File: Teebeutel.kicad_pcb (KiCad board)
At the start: 2 copper layers, 40 x 55.7 mm, 66 parts, among them J1 RJ45_Shielded, J2 Conn_01x30_Female, J3 Micro_SD_Card, Q1 S8050, Q2 S8050, SW1 K1-1506SN-01, U1 ESP32-WROOM-32, U2 TLV1117-33, U3 MCP73831-2-OT, U4 SDB628, U5 LIS2DE12, U6 TLV70018_SOT23-5, U7 SGP30, U8 PPSI262, U9 TXB0104RUT

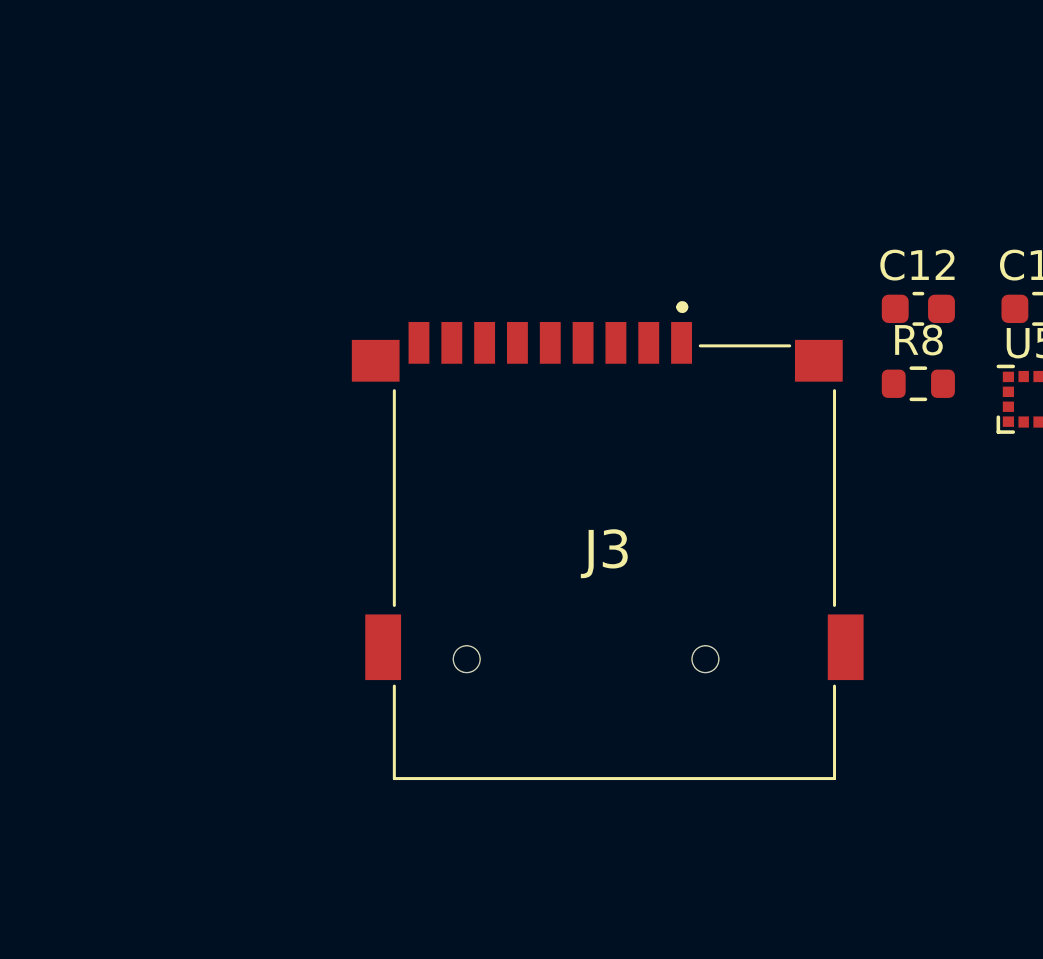
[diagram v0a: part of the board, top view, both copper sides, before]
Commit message: fix: Move pulldown R in the Boot-mode selector
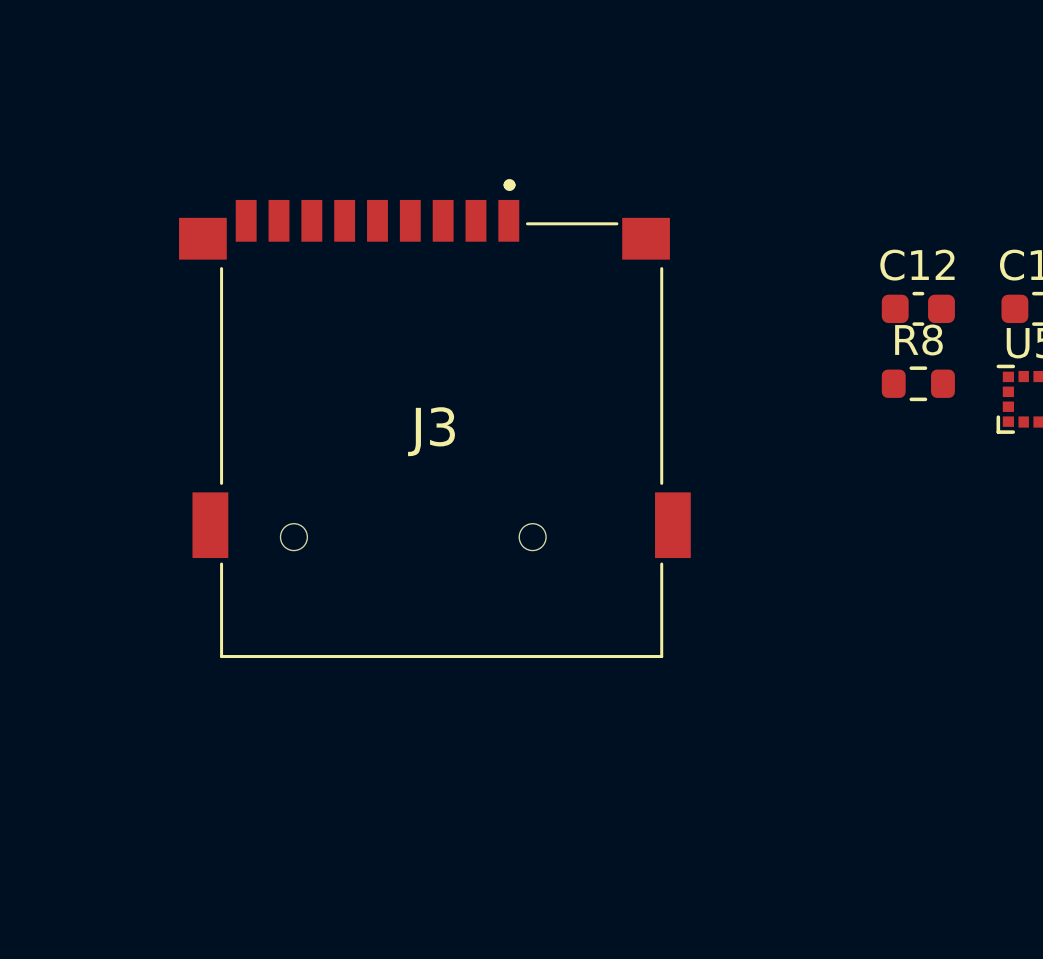
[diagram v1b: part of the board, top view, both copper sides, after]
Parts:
- moved J3 7.09 mm to (109.0, -20.4)
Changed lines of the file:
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@@
     (add_net WS2812)
+  )
+  (module custom_parts:TF15X15 (layer F.Cu)
+    (at 109 -20.4)
+    (descr TF-15X15-4)
+    (tags Connector)
+    (fp_text reference J3 (at 0 0) (layer F.SilkS)
+      (effects (font (size 1.27 1.27) (thickness 0.254)))
+    )
+    (fp_text value Micro_SD_Card (at 0 0) (layer F.SilkS) hide
+      (effects (font (size 1.27 1.27) (thickness 0.254)))
+    )
+    (fp_text user %R (at 0 0) (layer F.Fab)
+      (effects (font (size 1.27 1.27) (thickness 0.254)))
+    )
+    (fp_arc (start 2.5 -8.15) (end 2.4 -8.15) (angle -180) (layer F.SilkS) (width 0.2))
+    (fp_arc (start 2.5 -8.15) (end 2.6 -8.15) (angle -180) (layer F.SilkS) (width 0.2))
+    (fp_line (start 2.6 -8.15) (end 2.6 -8.15) (layer F.SilkS) (width 0.2))
+    (fp_line (start 2.4 -8.15) (end 2.4 -8.15) (layer F.SilkS) (width 0.2))
+    (fp_line (start 6.1 -6.85) (end 3.1 -6.85) (layer F.SilkS) (width 0.1))
+    (fp_line (start 7.6 1.85) (end 7.6 -5.35) (layer F.SilkS) (width 0.1))
+    (fp_line (start 7.6 7.65) (end 7.6 4.55) (layer F.SilkS) (width 0.1))
+    (fp_line (start -7.15 7.65) (end 7.6 7.65) (layer F.SilkS) (width 0.1))
+    (fp_line (start -7.15 4.55) (end -7.15 7.65) (layer F.SilkS) (width 0.1))
+    (fp_line (start -7.15 -5.35) (end -7.15 1.85) (layer F.SilkS) (width 0.1))
+    (fp_line (start -9.575 8.65) (end -9.575 -8.65) (layer F.CrtYd) (width 0.1))
+    (fp_line (start 9.575 8.65) (end -9.575 8.65) (layer F.CrtYd) (width 0.1))
+    (fp_line (start 9.575 -8.65) (end 9.575 8.65) (layer F.CrtYd) (width 0.1))
+    (fp_line (start -9.575 -8.65) (end 9.575 -8.65) (layer F.CrtYd) (width 0.1))
+    (fp_line (start -7.15 7.65) (end -7.15 -6.85) (layer F.Fab) (width 0.2))
+    (fp_line (start 7.6 7.65) (end -7.15 7.65) (layer F.Fab) (width 0.2))
+    (fp_line (start 7.6 -6.85) (end 7.6 7.65) (layer F.Fab) (width 0.2))
+    (fp_line (start -7.15 -6.85) (end 7.6 -6.85) (layer F.Fab) (width 0.2))
+    (pad 1 smd rect (at 2.475 -6.95) (size 0.7 1.4) (layers F.Cu F.Paste F.Mask))
+    (pad 2 smd rect (at 1.375 -6.95) (size 0.7 1.4) (layers F.Cu F.Paste F.Mask)
+      (net 29 SD-CS))
+    (pad 3 smd rect (at 0.275 -6.95) (size 0.7 1.4) (layers F.Cu F.Paste F.Mask)
+      (net 28 SD-MOSI))
+    (pad 4 smd rect (at -0.825 -6.95) (size 0.7 1.4) (layers F.Cu F.Paste F.Mask)
+      (net 9 +3V3))
+    (pad 5 smd rect (at -1.925 -6.95) (size 0.7 1.4) (layers F.Cu F.Paste F.Mask)
+      (net 27 SD-SCK))
+    (pad 6 smd rect (at -3.025 -6.95) (size 0.7 1.4) (layers F.Cu F.Paste F.Mask)
+      (net 2 GND))
+    (pad 7 smd rect (at -4.125 -6.95) (size 0.7 1.4) (layers F.Cu F.Paste F.Mask)
+      (net 26 SD-MISO))
+    (pad 8 smd rect (at -5.225 -6.95) (size 0.7 1.4) (layers F.Cu F.Paste F.Mask))
+    (pad 9 smd rect (at -6.325 -6.95) (size 0.7 1.4) (layers F.Cu F.Paste F.Mask)
+      (net 2 GND))
+    (pad 14 np_thru_hole circle (at -4.725 3.65) (size 0.9 0) (drill 0.9) (layers *.Cu *.Mask))
+    (pad 15 np_thru_hole circle (at 3.275 3.65) (size 0.9 0) (drill 0.9) (layers *.Cu *.Mask))
+    (pad MP1 smd rect (at -7.775 -6.35 90) (size 1.4 1.6) (layers F.Cu F.Paste F.Mask))
+    (pad MP2 smd rect (at 7.075 -6.35 90) (size 1.4 1.6) (layers F.Cu F.Paste F.Mask))
+    (pad MP3 smd rect (at -7.525 3.25) (size 1.2 2.2) (layers F.Cu F.Paste F.Mask))
+    (pad MP4 smd rect (at 7.975 3.25) (size 1.2 2.2) (layers F.Cu F.Paste F.Mask))
+    (model ${KIPRJMOD}/custom_parts.pretty/TF-15X15.stp
+      (offset (xyz 0.22 -0.11 0.97))
+      (scale (xyz 1 1 1))
+      (rotate (xyz -90 0 0))
+    )
   )
   (module custom_parts:K1-1506SN-01 (layer F.Cu)
@@
     )
   )
-  (module custom_parts:TF15X15 (layer F.Cu)
-    (at 114.79 -16.31)
-    (descr TF-15X15-4)
-    (tags Connector)
-    (fp_text reference J3 (at 0 0) (layer F.SilkS)
-      (effects (font (size 1.27 1.27) (thickness 0.254)))
-    )
-    (fp_text value Micro_SD_Card (at 0 0) (layer F.SilkS) hide
-      (effects (font (size 1.27 1.27) (thickness 0.254)))
-    )
-    (fp_text user %R (at 0 0) (layer F.Fab)
-      (effects (font (size 1.27 1.27) (thickness 0.254)))
-    )
-    (fp_arc (start 2.5 -8.15) (end 2.4 -8.15) (angle -180) (layer F.SilkS) (width 0.2))
-    (fp_arc (start 2.5 -8.15) (end 2.6 -8.15) (angle -180) (layer F.SilkS) (width 0.2))
-    (fp_line (start 2.6 -8.15) (end 2.6 -8.15) (layer F.SilkS) (width 0.2))
-    (fp_line (start 2.4 -8.15) (end 2.4 -8.15) (layer F.SilkS) (width 0.2))
-    (fp_line (start 6.1 -6.85) (end 3.1 -6.85) (layer F.SilkS) (width 0.1))
-    (fp_line (start 7.6 1.85) (end 7.6 -5.35) (layer F.SilkS) (width 0.1))
-    (fp_line (start 7.6 7.65) (end 7.6 4.55) (layer F.SilkS) (width 0.1))
-    (fp_line (start -7.15 7.65) (end 7.6 7.65) (layer F.SilkS) (width 0.1))
-    (fp_line (start -7.15 4.55) (end -7.15 7.65) (layer F.SilkS) (width 0.1))
-    (fp_line (start -7.15 -5.35) (end -7.15 1.85) (layer F.SilkS) (width 0.1))
-    (fp_line (start -9.575 8.65) (end -9.575 -8.65) (layer F.CrtYd) (width 0.1))
-    (fp_line (start 9.575 8.65) (end -9.575 8.65) (layer F.CrtYd) (width 0.1))
-    (fp_line (start 9.575 -8.65) (end 9.575 8.65) (layer F.CrtYd) (width 0.1))
-    (fp_line (start -9.575 -8.65) (end 9.575 -8.65) (layer F.CrtYd) (width 0.1))
-    (fp_line (start -7.15 7.65) (end -7.15 -6.85) (layer F.Fab) (width 0.2))
-    (fp_line (start 7.6 7.65) (end -7.15 7.65) (layer F.Fab) (width 0.2))
-    (fp_line (start 7.6 -6.85) (end 7.6 7.65) (layer F.Fab) (width 0.2))
-    (fp_line (start -7.15 -6.85) (end 7.6 -6.85) (layer F.Fab) (width 0.2))
-    (pad 1 smd rect (at 2.475 -6.95) (size 0.7 1.4) (layers F.Cu F.Paste F.Mask))
-    (pad 2 smd rect (at 1.375 -6.95) (size 0.7 1.4) (layers F.Cu F.Paste F.Mask)
-      (net 29 SD-CS))
-    (pad 3 smd rect (at 0.275 -6.95) (size 0.7 1.4) (layers F.Cu F.Paste F.Mask)
-      (net 28 SD-MOSI))
-    (pad 4 smd rect (at -0.825 -6.95) (size 0.7 1.4) (layers F.Cu F.Paste F.Mask)
-      (net 9 +3V3))
-    (pad 5 smd rect (at -1.925 -6.95) (size 0.7 1.4) (layers F.Cu F.Paste F.Mask)
-      (net 27 SD-SCK))
-    (pad 6 smd rect (at -3.025 -6.95) (size 0.7 1.4) (layers F.Cu F.Paste F.Mask)
-      (net 2 GND))
-    (pad 7 smd rect (at -4.125 -6.95) (size 0.7 1.4) (layers F.Cu F.Paste F.Mask)
-      (net 26 SD-MISO))
-    (pad 8 smd rect (at -5.225 -6.95) (size 0.7 1.4) (layers F.Cu F.Paste F.Mask))
-    (pad 9 smd rect (at -6.325 -6.95) (size 0.7 1.4) (layers F.Cu F.Paste F.Mask)
-      (net 2 GND))
-    (pad 14 np_thru_hole circle (at -4.725 3.65) (size 0.9 0) (drill 0.9) (layers *.Cu *.Mask))
-    (pad 15 np_thru_hole circle (at 3.275 3.65) (size 0.9 0) (drill 0.9) (layers *.Cu *.Mask))
-    (pad MP1 smd rect (at -7.775 -6.35 90) (size 1.4 1.6) (layers F.Cu F.Paste F.Mask))
-    (pad MP2 smd rect (at 7.075 -6.35 90) (size 1.4 1.6) (layers F.Cu F.Paste F.Mask))
-    (pad MP3 smd rect (at -7.525 3.25) (size 1.2 2.2) (layers F.Cu F.Paste F.Mask))
-    (pad MP4 smd rect (at 7.975 3.25) (size 1.2 2.2) (layers F.Cu F.Paste F.Mask))
-    (model ${KIPRJMOD}/custom_parts.pretty/TF-15X15.stp
-      (offset (xyz 0.22 -0.11 0.97))
-      (scale (xyz 1 1 1))
-      (rotate (xyz -90 0 0))
-    )
-  )

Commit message: feat: alot of stuff
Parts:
- added C20: 100n, Capacitor_SMD:C_0603_1608Metric, F.Cu at (121.8, 131.0)
- added C21: 10µ, Capacitor_SMD:C_0603_1608Metric, F.Cu at (240.5, 47.5)
- added C22: 1µ, Capacitor_SMD:C_0603_1608Metric, F.Cu at (256.1, 34.1)
- added C23: 10µ, Capacitor_SMD:C_0603_1608Metric, F.Cu at (232.1, 58.2)
- added C24: 100n, Capacitor_SMD:C_0603_1608Metric, F.Cu at (236.1, 53.8)
- added C25: 4,7µ, Capacitor_SMD:C_0603_1608Metric, F.Cu at (240.5, 50.0)
- added C26: 4,7µ, Capacitor_SMD:C_0603_1608Metric, F.Cu at (260.7, 29.7)
- added C27: 100n, Capacitor_SMD:C_0603_1608Metric, F.Cu at (121.5, 136.1)
- added C28: 22µF, Capacitor_SMD:C_0603_1608Metric, F.Cu at (246.7, 45.0)
- added C29: 10µ, Capacitor_SMD:C_0603_1608Metric, F.Cu at (252.5, 49.1)
- added C30: 100n, Capacitor_SMD:C_0603_1608Metric, F.Cu at (242.7, 42.5)
- added C31: 22µF, Capacitor_SMD:C_0603_1608Metric, F.Cu at (255.9, 36.6)
- added C32: 10µ, Capacitor_SMD:C_0603_1608Metric, F.Cu at (236.1, 56.3)
- added D10: WS2812B, Teebeutel_Special_Parts:WS2812B-4020, F.Cu at (111.0, 80.0)
- added D11: WS2812B, Teebeutel_Special_Parts:WS2812B-4020, F.Cu at (172.0, 149.0)
- added D12: WS2812B, Teebeutel_Special_Parts:WS2812B-4020, F.Cu at (120.6, 58.0)
- added D13: LED-RED, LED_SMD:LED_1210_3225Metric, F.Cu at (159.9, 52.5)
- added D14: LED-GREEN, LED_SMD:LED_1210_3225Metric, F.Cu at (132.1, 52.5)
- added D15: 1N4148WT, Diode_SMD:D_SOD-523, F.Cu at (272.5, 30.1)
- added D16: 1N4148WT, Diode_SMD:D_SOD-523, F.Cu at (247.9, 55.0)
- added D17: D, Diode_SMD:D_SMA, F.Cu at (212.4, 56.9)
- added G***: LOGO, Teebeutel_Graphics:rotate-orbit, F.Cu at (142.1, 100.0)
- added G***: LOGO, Teebeutel_Graphics:wind, B.Cu at (126.2, 139.2)
- added G***: LOGO, Teebeutel_Graphics:heartbeat, B.Cu at (165.8, 139.2)
- added J4: Conn_01x30_Female, Connector_FFC-FPC:TE_3-84953-0_1x30-1MP_P1.0mm_Horizontal, F.Cu at (146.0, 87.0)
- added R23: 560k, Resistor_SMD:R_0603_1608Metric, F.Cu at (252.5, 46.6)
- added R24: 620k 1%, Resistor_SMD:R_0603_1608Metric, F.Cu at (248.5, 52.5)
- added R25: 30k 1%, Resistor_SMD:R_0603_1608Metric, F.Cu at (268.2, 32.7)
- added SW2: SW_SPST, Button_Switch_SMD:SW_SPDT_PCM12, F.Cu at (113.0, 130.0)
- added TB1: Touch Button 2, Teebeutel_Graphics:Touch-Button_Python, B.Cu at (120.0, 120.0)
- added TB2: Touch Button 2, Teebeutel_Graphics:Touch-Button_OSHW, B.Cu at (172.0, 120.0)
- added TP1: ESP32 EN, TestPoint:TestPoint_Pad_D1.0mm, F.Cu at (262.2, 42.5)
- added TP10: RxD 3.3V, TestPoint:TestPoint_Pad_D1.0mm, F.Cu at (259.1, 48.1)
- added TP11: RTS 3.3V, TestPoint:TestPoint_Pad_D1.0mm, F.Cu at (256.1, 48.1)
- added TP12: Button Right, TestPoint:TestPoint_Pad_D1.0mm, F.Cu at (266.7, 38.5)
- added TP13: I²C SDA, TestPoint:TestPoint_Pad_D1.0mm, F.Cu at (251.2, 55.3)
- added TP14: I²C SCL, TestPoint:TestPoint_Pad_D1.0mm, F.Cu at (275.8, 31.0)
- added TP15: TestPoint, TestPoint:TestPoint_Pad_D1.0mm, F.Cu at (256.1, 51.1)
- added TP16: TestPoint, TestPoint:TestPoint_Pad_D1.0mm, F.Cu at (262.1, 45.5)
- added TP17: SD-Card CS, TestPoint:TestPoint_Pad_D1.0mm, F.Cu at (249.9, 58.4)
- added TP18: SD-Card MISO, TestPoint:TestPoint_Pad_D1.0mm, F.Cu at (254.2, 55.0)
- added TP19: SD-Card MOSI, TestPoint:TestPoint_Pad_D1.0mm, F.Cu at (274.7, 34.0)
- added TP2: WS2821, TestPoint:TestPoint_Pad_D1.0mm, F.Cu at (120.0, 146.2)
- added TP20: SD-Card SCK, TestPoint:TestPoint_Pad_D1.0mm, F.Cu at (269.8, 39.0)
- added TP21: Charging status, TestPoint:TestPoint_Pad_D1.0mm, F.Cu at (135.0, 63.2)
- added TP22: ADC Battery (1/4 Battery voltage), TestPoint:TestPoint_Pad_D1.0mm, F.Cu at (257.3, 54.2)
- added TP23: V +1.8V, TestPoint:TestPoint_Pad_D1.0mm, F.Cu at (253.0, 58.4)
- added TP24: OLED VPP (13V), TestPoint:TestPoint_Pad_D1.0mm, F.Cu at (272.8, 39.0)
- added TP25: OLED SDA, TestPoint:TestPoint_Pad_D1.0mm, F.Cu at (268.4, 42.1)
- added TP26: OLED SCK, TestPoint:TestPoint_Pad_D1.0mm, F.Cu at (265.3, 41.7)
- added TP27: OLED CS, TestPoint:TestPoint_Pad_D1.0mm, F.Cu at (268.4, 45.1)
- added TP28: OLED DC, TestPoint:TestPoint_Pad_D1.0mm, F.Cu at (271.4, 42.1)
- added TP29: OLED RESET, TestPoint:TestPoint_Pad_D1.0mm, F.Cu at (262.1, 51.6)
- added TP3: ESP32 IO0, TestPoint:TestPoint_Pad_D1.0mm, F.Cu at (252.0, 51.9)
- added TP30: V +3.3V, TestPoint:TestPoint_Pad_D1.0mm, F.Cu at (265.2, 47.8)
- added TP4: Button Down, TestPoint:TestPoint_Pad_D1.0mm, F.Cu at (258.2, 45.0)
- added TP5: Button Left, TestPoint:TestPoint_Pad_D1.0mm, F.Cu at (276.3, 27.9)
- added TP6: Button Up, TestPoint:TestPoint_Pad_D1.0mm, F.Cu at (223.6, 56.2)
- added TP7: Button Push, TestPoint:TestPoint_Pad_D1.0mm, F.Cu at (246.9, 57.8)
- added TP8: DTR 3.3V, TestPoint:TestPoint_Pad_D1.0mm, F.Cu at (271.7, 32.9)
- added TP9: TxD 3.3V, TestPoint:TestPoint_Pad_D1.0mm, F.Cu at (270.7, 36.0)
- added U10: TLV1117-33, Package_TO_SOT_SMD:SOT-223, F.Cu at (121.5, 126.0)
- C1, C2, C5, C7: value 10µ -> 100n; moved to F.Cu
- C10, C9: value 4,7µ -> 100n; moved to F.Cu
- C11, C3: value 22µF -> 100n; moved to F.Cu
- C13, C15: value 10µ -> 100n
- C18: value 100n -> 10µ
- C19: value 100n -> 1µ
- C4: value 1µ -> 100n; moved to F.Cu
- C6: value 1µ -> 10µ; moved to F.Cu
- C8, L1, R1, R2: moved to F.Cu
- D1, D2: value 1N4148WT -> WS2812B; footprint Diode_SMD:D_SOD-523 -> Teebeutel_Special_Parts:WS2812B-4020; moved to F.Cu
- D3: value D -> WS2812B; footprint Diode_SMD:D_SMA -> Teebeutel_Special_Parts:WS2812B-4020; moved to F.Cu
- D4, D7, D8, D9: footprint LED_SMD:LED_WS2812B_PLCC4_5.0x5.0mm_P3.2mm -> Teebeutel_Special_Parts:WS2812B-4020
- D5, D6: value LED -> WS2812B; footprint LED_SMD:LED_1210_3225Metric -> Teebeutel_Special_Parts:WS2812B-4020
- J2: value Conn_01x30_Female -> Micro_SD_Card; footprint Connector_FFC-FPC:TE_3-84953-0_1x30-1MP_P1.0mm_Horizontal -> Teebeutel_Special_Parts:TF15X15; moved to F.Cu
- J3: value Micro_SD_Card -> Battery; footprint custom_parts:TF15X15 -> Connector_PinHeader_2.54mm:PinHeader_1x02_P2.54mm_Vertical
- Q1, Q2: footprint Package_TO_SOT_THT:TO-92_Inline -> Package_TO_SOT_SMD:SOT-23
- R10, R9: value 470 -> 10k
- R16: value 10k -> 2k2
- R18, R19: value 10k -> 470
- R20: value 10k -> 300k
- R21: value 10k -> 100k
- R22: value 10k -> 50
- R3: value 2k2 -> 10k; moved to F.Cu
- R4: value 50 -> 10k; moved to F.Cu
- R5: value 620k 1% -> 10k; moved to F.Cu
- R6: value 30k 1% -> 10k; moved to F.Cu
- R7: value 560k -> 10k; moved to F.Cu
- SW1: footprint custom_parts:K1-1506SN-01 -> Teebeutel_Special_Parts:K1-1506SN-01; moved to B.Cu
- U1: value ESP32-WROOM-32 -> LIS2DE12; footprint RF_Module:ESP32-WROOM-32 -> Package_LGA:LGA-12_2x2mm_P0.5mm; moved to F.Cu
- U2: value TLV1117-33 -> ESP32-WROOM-32; footprint Package_TO_SOT_SMD:SOT-223 -> RF_Module:ESP32-WROOM-32; moved to F.Cu
- U3: value MCP73831-2-OT -> TXB0104RUT; footprint Package_TO_SOT_SMD:SOT-23-5 -> Package_DFN_QFN:Texas_R_PUQFN-N12; moved to F.Cu
- U4: value SDB628 -> TXB0104RUT; footprint Package_TO_SOT_SMD:SOT-23-6 -> Package_DFN_QFN:Texas_R_PUQFN-N12; moved to F.Cu
- U5: value LIS2DE12 -> SGP30; footprint Package_LGA:LGA-12_2x2mm_P0.5mm -> Teebeutel_Special_Parts:SGP30; moved to B.Cu
- U6: value TLV70018_SOT23-5 -> PPSI262; footprint Package_TO_SOT_SMD:SOT-23-5 -> Teebeutel_Special_Parts:PPSI262; moved to B.Cu
- U7: value SGP30 -> MCP73831-2-OT; footprint custom_parts:SGP30 -> Package_TO_SOT_SMD:SOT-23-5
- U8: value PPSI262 -> TLV70018_SOT23-5; footprint custom_parts:PPSI262 -> Package_TO_SOT_SMD:SOT-23-5
- U9: value TXB0104RUT -> SDB628; footprint Package_DFN_QFN:Texas_R_PUQFN-N12 -> Package_TO_SOT_SMD:SOT-23-6
- moved D4 327.5 mm to (111.0, 140.0), turned to 90 degrees
- moved U6 320.8 mm to (165.8, 135.0), turned to 180 degrees
- moved D6 316.4 mm to (111.0, 120.0), turned to 90 degrees
- moved R12 311.7 mm to (133.2, 138.2), turned to 90 degrees
- moved SW1 306.7 mm to (146.0, 125.0)
- moved R11 306.2 mm to (126.2, 144.0)
- moved U8 301.3 mm to (118.7, 136.2)
- moved U9 300.0 mm to (170.3, 116.4)
- moved D8 298.5 mm to (111.0, 100.0), turned to 90 degrees
- moved R9 295.9 mm to (144.2, 120.8), turned to 270 degrees
- moved D9 294.8 mm to (181.0, 140.0), turned to 270 degrees
- moved R21 293.2 mm to (118.8, 132.5), turned to 180 degrees
- moved R10 291.3 mm to (149.2, 120.8), turned to 270 degrees
- moved R15 289.2 mm to (274.0, 25.1)
- moved Q1 289.1 mm to (247.7, 37.5)
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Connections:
- C1 pad 1: +5V -> +3V3
- C10 pad 1: Net-(C10-Pad1) -> +3V3
- C11 pad 1: VPP -> +3V3
- C14 pad 1: +1V8 -> +3V3
- C15 pad 1: +1V8 -> +3V3
- C16 pad 1: +3V3 -> Net-(C16-Pad1)
- C17 pad 1: +3V3 -> +5V
- C18 pad 1: +3V3 -> Net-(C18-Pad1)
- C2 pad 1: +BATT -> +3V3
- C4 pad 1: Net-(C4-Pad1) -> +3V3
- C5 pad 1: VPP -> +3V3
- C6 pad 1: Net-(C6-Pad1) -> +3V3
- C7 pad 1: Net-(C10-Pad1) -> +3V3
- C8 pad 1: VPP -> +3V3
- C9 pad 1: Net-(C9-Pad1) -> +3V3
- D1 pad 2: Net-(D1-Pad2) -> +3V3
- D2 pad 1: GND -> WS2812
- D2 pad 2: Net-(D1-Pad1) -> +3V3
- D3 pad 1: VPP -> Net-(D1-Pad3)
- D3 pad 2: Net-(D3-Pad2) -> +3V3
- D4 pad 1: +3V3 -> Net-(D2-Pad3)
- D4 pad 2: Net-(D4-Pad2) -> +3V3
- D4 pad 3: GND -> Net-(D4-Pad3)
- D4 pad 4: WS2812 -> GND
- D5 pad 1: Net-(D5-Pad1) -> Net-(D3-Pad3)
- D5 pad 2: Net-(D5-Pad2) -> +3V3
- D6 pad 1: Net-(D6-Pad1) -> Net-(D4-Pad3)
- D6 pad 2: Net-(D5-Pad1) -> +3V3
- D7 pad 1: +3V3 -> Net-(D5-Pad3)
- D7 pad 2: Net-(D7-Pad2) -> +3V3
- D7 pad 3: GND -> Net-(D7-Pad3)
- D7 pad 4: Net-(D4-Pad2) -> GND
- D8 pad 1: +3V3 -> Net-(D6-Pad3)
- D8 pad 2: Net-(D8-Pad2) -> +3V3
- D8 pad 3: GND -> Net-(D10-Pad1)
- D8 pad 4: Net-(D7-Pad2) -> GND
- D9 pad 1: +3V3 -> Net-(D7-Pad3)
- D9 pad 2: (no net) -> +3V3
- D9 pad 3: GND -> Net-(D11-Pad1)
- D9 pad 4: Net-(D8-Pad2) -> GND
- J1 pad 3: RTS -> Net-(J1-Pad3)
- J1 pad 4: RxD -> Net-(J1-Pad4)
- J1 pad 5: TxD -> Net-(J1-Pad5)
- J1 pad 6: DTR -> Net-(J1-Pad6)
- J2 pad 1: GND -> (no net)
- J2 pad 14: +3V3 -> (no net)
- J2 pad 15: GND -> (no net)
- J2 pad 2: (no net) -> SD-CS
- J2 pad 3: GND -> SD-MOSI
- J2 pad 4: Net-(C10-Pad1) -> +3V3
- J2 pad 5: Net-(C4-Pad1) -> SD-SCK
- J2 pad 6: (no net) -> GND
- J2 pad 7: (no net) -> SD-MISO
- J2 pad 9: Net-(J2-Pad9) -> GND
- J3 pad 1: (no net) -> GND
- J3 pad 2: SD-CS -> Net-(C18-Pad1)
- L1 pad 2: Net-(D3-Pad2) -> Net-(D17-Pad2)
- Q1 pad 2: Net-(Q1-Pad2) -> RTS
- Q1 pad 3: RTS -> Net-(Q1-Pad3)
- Q2 pad 1: DTR -> Net-(Q2-Pad1)
- Q2 pad 2: Net-(Q2-Pad2) -> DTR
- R1 pad 2: Net-(Q1-Pad1) -> Net-(R1-Pad2)
- R10 pad 1: Net-(D6-Pad1) -> +3V3
- R10 pad 2: GND -> BTN_PUSH
- R11 pad 1: +3V3 -> Net-(R11-Pad1)
- R11 pad 2: BTN_DOWN -> GND
- R12 pad 2: BTN_LEFT -> BTN_RIGHT
- R13 pad 2: BTN_UP -> I2C-SDA
- R14 pad 1: +3V3 -> Net-(R14-Pad1)
- R14 pad 2: BTN_PUSH -> GND
- R15 pad 2: BTN_RIGHT -> I2C-SCL
- R18 pad 1: Net-(R18-Pad1) -> +5V
- R18 pad 2: GND -> Net-(D13-Pad2)
- R19 pad 1: +3V3 -> Net-(D14-Pad1)
- R19 pad 2: I2C-SDA -> GND
- R2 pad 1: +3V3 -> GND
- R2 pad 2: Net-(Q2-Pad3) -> RTS
- R20 pad 1: +3V3 -> +BATT
- R20 pad 2: I2C-SCL -> ADC-BAT
- R21 pad 1: Net-(Q1-Pad2) -> ADC-BAT
- R21 pad 2: DTR -> GND
- R22 pad 1: Net-(Q2-Pad2) -> Net-(D15-Pad2)
- R22 pad 2: RTS -> Net-(J4-Pad26)
- R3 pad 1: Net-(R3-Pad1) -> GND
- R3 pad 2: GND -> DTR
- R4 pad 1: Net-(D1-Pad2) -> Net-(Q1-Pad1)
- R4 pad 2: Net-(J2-Pad26) -> DTR
- R5 pad 1: Net-(R5-Pad1) -> Net-(Q2-Pad1)
- R5 pad 2: VPP -> RTS
- R6 pad 1: Net-(R5-Pad1) -> +3V3
- R6 pad 2: GND -> BTN_DOWN
- R7 pad 1: Net-(J2-Pad9) -> Net-(R7-Pad1)
- R8 pad 2: Net-(R8-Pad2) -> BTN_LEFT
- R9 pad 1: +5V -> +3V3
- R9 pad 2: Net-(D5-Pad2) -> BTN_UP
- U1 pad 1: GND -> I2C-SCL
- U1 pad 10: (no net) -> +3V3
- U1 pad 2: +3V3 -> Net-(R1-Pad2)
- U1 pad 3: Net-(Q1-Pad1) -> (no net)
- U1 pad 4: (no net) -> I2C-SDA
- U1 pad 5: (no net) -> GND
- U1 pad 6: (no net) -> GND
- U1 pad 7: (no net) -> GND
- U1 pad 8: (no net) -> GND
- U1 pad 9: (no net) -> +3V3
- U2 pad 3: +BATT -> Net-(Q1-Pad3)
- U2 pad 4: (no net) -> ADC-BAT
- U3 pad 1: Net-(D5-Pad1) -> +5V
- U3 pad 2: GND -> Net-(J1-Pad6)
- U3 pad 3: +BATT -> Net-(J1-Pad5)
- U3 pad 4: +5V -> Net-(J1-Pad4)
- U3 pad 5: Net-(R3-Pad1) -> Net-(J1-Pad3)
- U4 pad 1: Net-(D3-Pad2) -> +3V3
- U4 pad 2: GND -> I2C-SDA
- U4 pad 3: Net-(R5-Pad1) -> I2C-SCL
- U4 pad 4: +3V3 -> (no net)
- U4 pad 5: +3V3 -> (no net)
- U4 pad 6: (no net) -> GND
- U5 pad 1: I2C-SCL -> +1V8
- U5 pad 2: Net-(R8-Pad2) -> GND
- U5 pad 3: (no net) -> Net-(TP15-Pad1)
- U5 pad 4: I2C-SDA -> (no net)
- U5 pad 5: GND -> +1V8
- U5 pad 6: GND -> Net-(TP16-Pad1)
- U6 pad 1: +BATT -> (no net)
- U6 pad 2: GND -> (no net)
- U6 pad 3: +BATT -> Net-(C16-Pad1)
- U6 pad 5: +1V8 -> +3V3
- U7 pad 1: +1V8 -> Net-(D13-Pad1)
- U7 pad 3: Net-(U7-Pad3) -> Net-(C18-Pad1)
- U7 pad 4: (no net) -> +5V
- U7 pad 5: +1V8 -> Net-(R16-Pad1)
- U8 pad 1: (no net) -> +BATT
- U8 pad 2: (no net) -> GND
- U8 pad 3: Net-(C19-Pad1) -> +BATT
- U8 pad 5: +3V3 -> +1V8
- U9 pad 1: +3V3 -> Net-(D17-Pad2)
- U9 pad 2: I2C-SDA -> GND
- U9 pad 3: I2C-SCL -> Net-(R24-Pad1)
- U9 pad 4: (no net) -> +3V3
- U9 pad 5: (no net) -> +3V3
- U9 pad 6: GND -> (no net)
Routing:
- net Net-(C18-Pad1): track 0.00 -> 73.4 mm
- net +5V: track 0.00 -> 56.8 mm, vias 0 -> 1
- net Net-(D13-Pad1): track 0.00 -> 46.4 mm
- net BTN_RIGHT: track 0.00 -> 32.3 mm, vias 0 -> 1
- net Net-(D10-Pad3): track 0.00 -> 31.1 mm
- net WS2812: track 0.00 -> 31.1 mm
- net Net-(D10-Pad1): track 0.00 -> 27.2 mm
- net Net-(D6-Pad3): track 0.00 -> 27.0 mm
- net Net-(D4-Pad3): track 0.00 -> 26.3 mm
- net I2C-SDA: track 0.00 -> 20.1 mm, vias 0 -> 2
- net BTN_LEFT: track 0.00 -> 17.7 mm, vias 0 -> 1
- net I2C-SCL: track 0.00 -> 16.9 mm
- net Net-(D2-Pad3): track 0.00 -> 16.8 mm
- net +BATT: track 0.00 -> 16.2 mm
- net +1V8: track 0.00 -> 16.0 mm, vias 0 -> 1
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- added copper zone on B.Cu, net GND
- added copper zone on F.Cu, net GND
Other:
- board size 40 x 55.7 mm -> 72 x 100 mm
- net class Default: clearance 0.2 -> 0.127
- rule trace_clearance: 0.2 -> 0.127
- board text added: "+"
- board text added: "-"
- board text added: "3.7V"
- board text added: "CHARGING"
- board text added: "FULLY CHARGED"
- board text added: "LiPo Battery"
- board text added: "OLED 128x128"
- board text removed: "1,5" OLED"

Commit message: feat(): Finished routing and some clean up
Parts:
- added R26: 10, Resistor_SMD:R_0603_1608Metric, F.Cu at (162.8, 132.6)
- added REF**: KiCad-Logo2_5mm_SilkScreen, Symbol:KiCad-Logo2_5mm_SilkScreen, F.Cu at (158.8, 117.3)
- moved C5 190.0 mm to (112.2, 143.4), turned to 270 degrees
- moved C2 185.8 mm to (123.2, 148.0)
- moved TP5 177.1 mm to (134.8, 134.4)
- moved R4 175.9 mm to (129.8, 128.8), turned to 270 degrees
- moved TP12 167.1 mm to (134.8, 141.0), turned to 180 degrees
- moved C12 165.7 mm to (112.0, 83.8), turned to 270 degrees
- moved Q2 163.6 mm to (133.6, 125.4), turned to 180 degrees
- moved TP30 162.2 mm to (116.4, 112.2)
- moved TP16 162.1 mm to (126.8, 134.8)
- moved C29 161.1 mm to (118.8, 139.0), turned to 180 degrees
- moved R15 159.9 mm to (164.0, 141.2), turned to 90 degrees
- moved TP1 159.9 mm to (129.4, 131.4), turned to 180 degrees
- moved R2 159.4 mm to (129.0, 122.8)
- moved R25 158.4 mm to (133.6, 116.2), turned to 270 degrees
- moved TP15 157.0 mm to (122.4, 133.4)
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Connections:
- J2 pad 5: SD-SCK -> Net-(J2-Pad5)
- TP20 pad 1: SD-SCK -> Net-(J2-Pad5)
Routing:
- net +3V3: track 3.47 -> 545.5 mm, vias 0 -> 27
- net TxD: track 0.90 -> 107.5 mm, vias 0 -> 6
- net RxD: track 0.90 -> 104.5 mm, vias 0 -> 6
- net DTR: track 0.90 -> 95.0 mm
- net I2C-SCL: track 16.9 -> 106.2 mm, vias 0 -> 9
- net RTS: track 0.90 -> 87.5 mm, vias 0 -> 2
- net I2C-SDA: track 20.1 -> 100.5 mm, vias 2 -> 8
- net Net-(D1-Pad1): track 0.00 -> 61.8 mm, vias 0 -> 2
- net OLED-DC: track 0.00 -> 59.1 mm, vias 0 -> 2
- net OLED-RES: track 0.00 -> 59.0 mm, vias 0 -> 4
- net OLED-CS: track 0.00 -> 53.0 mm, vias 0 -> 4
- net OLED-SDA: track 0.00 -> 48.0 mm
- net VPP: track 0.00 -> 46.8 mm
- net OLED-SCK: track 0.00 -> 45.5 mm
- net ADC-BAT: track 2.90 -> 44.1 mm, vias 0 -> 2
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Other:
- board text added: "JLCJLCJLCJLC"
- board text added: "Teebeutel v0.1"
- board text added: "teebeutel.jadyn.dev"
